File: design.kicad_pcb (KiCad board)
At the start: 2 copper layers, 28.5 x 15 mm, 15 parts, among them J1 USB_C_Receptacle, J2 Conn_01x05, Q1 2N7002K, Q2 2N7002K, Q3 2N7002K, U1 ATtiny814-SS

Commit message: update
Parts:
- moved J2 20.1 mm to (151.5, 92.5), turned to 0 degrees
- moved C1 5.79 mm to (148.2, 81.0), turned to 180 degrees
- moved C2 5.76 mm to (151.6, 81.0)
- moved U1 0.75 mm to (151.5, 86.5)
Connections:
- C1 pad 1: Net-(C1-Pad1) -> VCC
- C1 pad 2: Net-(C1-Pad2) -> GND
- C2 pad 1: Net-(C2-Pad1) -> VCC
- C2 pad 2: Net-(C2-Pad2) -> GND
- J2 pad 1: Net-(J2-Pad1) -> UDPI
- J2 pad 2: Net-(J2-Pad2) -> VCC
- J2 pad 3: Net-(J2-Pad3) -> GND
- J2 pad 4: Net-(J2-Pad4) -> TX
- J2 pad 5: Net-(J2-Pad5) -> RX
- U1 pad 1: Net-(U1-Pad1) -> VCC
- U1 pad 10: Net-(U1-Pad10) -> UDPI
- U1 pad 11: Net-(U1-Pad11) -> TX
- U1 pad 12: Net-(U1-Pad12) -> RX
- U1 pad 13: Net-(U1-Pad13) -> WS2812b
- U1 pad 14: Net-(U1-Pad14) -> GND
- U1 pad 2: Net-(U1-Pad2) -> Blue_PWM
- U1 pad 3: Net-(U1-Pad3) -> Green_PWM
- U1 pad 6: Net-(U1-Pad6) -> Red_PWM

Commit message: PCB: change usb footprint add components
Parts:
- added R4: R_Small, Resistor_SMD:R_0805_2012Metric, F.Cu at (146.9, 72.0)
- added R5: 5.1k, Resistor_SMD:R_0805_2012Metric, F.Cu at (146.9, 75.0)
- added R6: 5.1k, Resistor_SMD:R_0805_2012Metric, F.Cu at (151.3, 72.0)
- added R7: R_Small, Resistor_SMD:R_0805_2012Metric, F.Cu at (151.3, 75.0)
- added R8: R_Small, Resistor_SMD:R_0805_2012Metric, F.Cu at (155.7, 72.0)
- J1: footprint Connector_USB:USB_C_Receptacle_HRO_TYPE-C-31-M-12 -> Connector_USB:USB_C_Receptacle_HRO_TYPE-C-31-M-12_simple
- J2: footprint E32-xxxT20D:UDPI_interface -> E32-xxxT20D:UDPI_interface_small
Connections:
- J1 pad A1: Net-(J1-PadA1) -> GND
- J1 pad A12: Net-(J1-PadA1) -> GND
- J1 pad A4: Net-(J1-PadA4) -> VCC
- J1 pad A9: Net-(J1-PadA4) -> VCC
- J1 pad B1: Net-(J1-PadA1) -> GND
- J1 pad B12: Net-(J1-PadA1) -> GND
- J1 pad B4: Net-(J1-PadA4) -> VCC
- J1 pad B9: Net-(J1-PadA4) -> VCC
- J1 pad S1: Net-(J1-PadS1) -> GND
- Q1 pad 1: Red_PWM -> Net-(Q1-Pad1)
- Q2 pad 1: Green_PWM -> Net-(Q2-Pad1)
- Q3 pad 1: Blue_PWM -> Net-(Q3-Pad1)
- R1 pad 1: Red_PWM -> Net-(Q1-Pad1)
- R2 pad 1: Green_PWM -> Net-(Q2-Pad1)
- R3 pad 1: Blue_PWM -> Net-(Q3-Pad1)

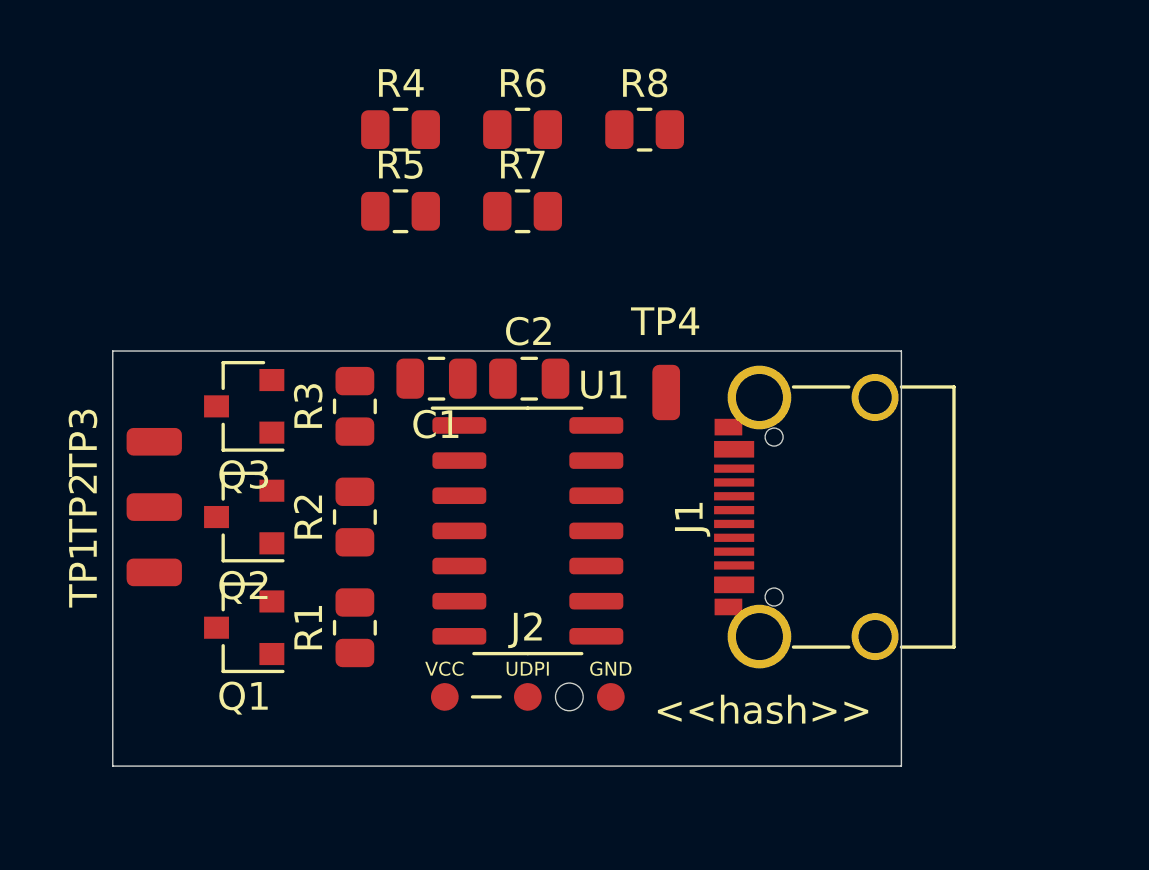
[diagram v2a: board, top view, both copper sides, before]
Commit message: PCB: move components
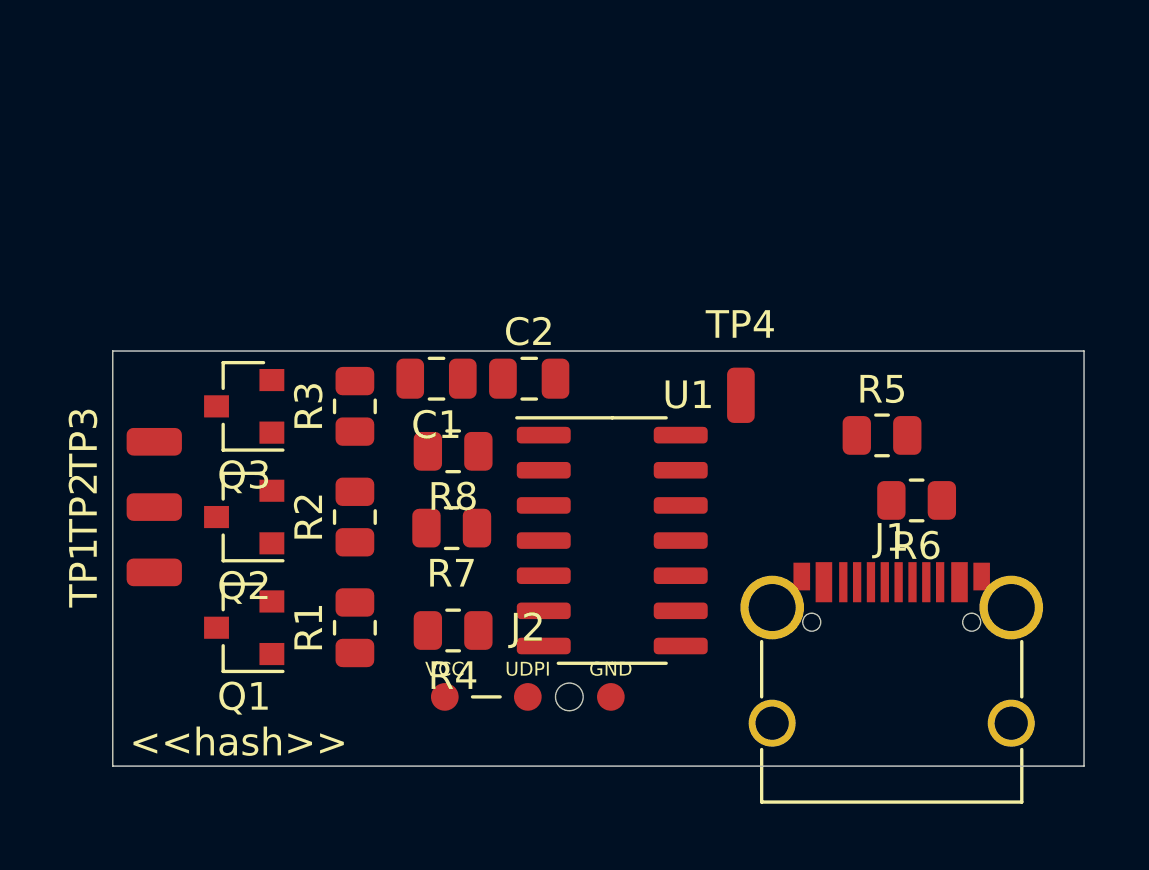
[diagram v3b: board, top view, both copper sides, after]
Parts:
- moved R6 19.6 mm to (165.6, 85.4), turned to 180 degrees
- moved R5 19.2 mm to (164.3, 83.0)
- moved R4 18.2 mm to (148.8, 90.1), turned to 180 degrees
- moved R8 13.5 mm to (148.8, 83.6), turned to 180 degrees
- moved R7 11.7 mm to (148.8, 86.4), turned to 180 degrees
- moved J1 6.61 mm to (164.7, 92.4), turned to 0 degrees
- moved U1 3.07 mm to (154.6, 86.8)
- moved TP4 2.70 mm to (159.2, 81.6)
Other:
- board size 28.5 x 15 mm -> 35.1 x 15 mm

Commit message: PCB: arrange
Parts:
- moved TP4 10.6 mm to (169.8, 81.4)
- moved C1 4.60 mm to (152.8, 81.2)
- moved C2 4.60 mm to (156.2, 81.2)
- moved J2 3.08 mm to (154.5, 93.2), turned to 180 degrees
- moved TP1 2.00 mm to (138.0, 90.0)
- moved TP3 1.28 mm to (138.0, 82.0)
- moved R5 0.50 mm to (164.3, 83.5)
- moved R6 0.50 mm to (165.6, 85.9)
- moved R8 0.43 mm to (148.8, 83.2)
- moved R4 0.42 mm to (148.7, 89.7)
- moved TP2 0.36 mm to (138.0, 86.0)
- moved R7 0.10 mm to (148.8, 86.5)
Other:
- board text added: "Blue"
- board text added: "Green"
- board text added: "Red"
- board text added: "WS2812B"
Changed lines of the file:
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@@
   (general
     (thickness 1.6)
-    (drawings 6)
+    (drawings 10)
     (tracks 0)
     (zones 0)
@@
     (47 F.CrtYd user)
     (48 B.Fab user)
-    (49 F.Fab user)
+    (49 F.Fab user hide)
   )
   (setup
@@
   )
   (module Resistor_SMD:R_0805_2012Metric (layer F.Cu)
-    (at 148.8 83.625 180)
+    (at 148.7875 83.2 180)
     (descr "Resistor SMD 0805 (2012 Metric), square (rectangular) end terminal, IPC_7351 nominal, (Body size source: IPC-SM-782 page 72, https://www.pcb-3d.com/wordpress/wp-content/uploads/ipc-sm-782a_amendment_1_and_2.pdf), generated with kicad-footprint-generator")
     (tags resistor)
@@
   )
   (module Resistor_SMD:R_0805_2012Metric (layer F.Cu)
-    (at 148.75 86.4 180)
+    (at 148.75 86.5 180)
     (descr "Resistor SMD 0805 (2012 Metric), square (rectangular) end terminal, IPC_7351 nominal, (Body size source: IPC-SM-782 page 72, https://www.pcb-3d.com/wordpress/wp-content/uploads/ipc-sm-782a_amendment_1_and_2.pdf), generated with kicad-footprint-generator")
     (tags resistor)
@@
   )
   (module Resistor_SMD:R_0805_2012Metric (layer F.Cu)
-    (at 165.55 85.4 180)
+    (at 165.55 85.9 180)
     (descr "Resistor SMD 0805 (2012 Metric), square (rectangular) end terminal, IPC_7351 nominal, (Body size source: IPC-SM-782 page 72, https://www.pcb-3d.com/wordpress/wp-content/uploads/ipc-sm-782a_amendment_1_and_2.pdf), generated with kicad-footprint-generator")
     (tags resistor)
     (attr smd)
-    (fp_text reference R6 (at 0 -1.65) (layer F.SilkS)
+    (fp_text reference R6 (at 2.65 -0.1) (layer F.SilkS)
       (effects (font (size 1 1) (thickness 0.15)))
     )
@@
   )
   (module Resistor_SMD:R_0805_2012Metric (layer F.Cu)
-    (at 164.3 83.05)
+    (at 164.3 83.55)
     (descr "Resistor SMD 0805 (2012 Metric), square (rectangular) end terminal, IPC_7351 nominal, (Body size source: IPC-SM-782 page 72, https://www.pcb-3d.com/wordpress/wp-content/uploads/ipc-sm-782a_amendment_1_and_2.pdf), generated with kicad-footprint-generator")
     (tags resistor)
     (attr smd)
-    (fp_text reference R5 (at 0 -1.65) (layer F.SilkS)
+    (fp_text reference R5 (at 2.7 -0.05) (layer F.SilkS)
       (effects (font (size 1 1) (thickness 0.15)))
     )
@@
   )
   (module Resistor_SMD:R_0805_2012Metric (layer F.Cu)
-    (at 148.8 90.1 180)
+    (at 148.6875 89.7 180)
     (descr "Resistor SMD 0805 (2012 Metric), square (rectangular) end terminal, IPC_7351 nominal, (Body size source: IPC-SM-782 page 72, https://www.pcb-3d.com/wordpress/wp-content/uploads/ipc-sm-782a_amendment_1_and_2.pdf), generated with kicad-footprint-generator")
     (tags resistor)
@@
   )
   (module E32-xxxT20D:UDPI_interface_small (layer F.Cu)
-    (at 151.5 92.5)
+    (at 154.5 93.2 180)
     (fp_text reference J2 (at 0 -2.5) (layer F.SilkS)
       (effects (font (size 1 1) (thickness 0.15)))
@@
     )
     (fp_line (start -2 0) (end -1 0) (layer F.SilkS) (width 0.12))
-    (pad "" np_thru_hole circle (at 1.5 0) (size 1 1) (drill 1) (layers *.Cu *.Mask))
-    (pad 3 smd circle (at 3 0) (size 1 1) (layers F.Cu F.Paste F.Mask)
-      (net 15 GND))
-    (pad 2 smd circle (at -3 0) (size 1 1) (layers F.Cu F.Paste F.Mask)
+    (pad "" np_thru_hole circle (at 1.5 0 180) (size 1 1) (drill 1) (layers *.Cu *.Mask))
+    (pad 3 smd circle (at 3 0 180) (size 1 1) (layers F.Cu F.Paste F.Mask)
+      (net 15 GND))
+    (pad 2 smd circle (at -3 0 180) (size 1 1) (layers F.Cu F.Paste F.Mask)
       (net 22 VCC))
-    (pad 1 smd circle (at 0 0) (size 1 1) (layers F.Cu F.Paste F.Mask)
+    (pad 1 smd circle (at 0 0 180) (size 1 1) (layers F.Cu F.Paste F.Mask)
       (net 25 UDPI))
   )
@@
     (tags "usb usb-c 2.0 pd")
     (attr smd)
-    (fp_text reference J1 (at 0 -5.645) (layer F.SilkS)
+    (fp_text reference J1 (at 6.15 -5.2) (layer F.SilkS)
       (effects (font (size 1 1) (thickness 0.15)))
     )
@@
     (tags "SOIC SO")
     (attr smd)
-    (fp_text reference U1 (at 2.75 -5.25) (layer F.SilkS)
+    (fp_text reference U1 (at 4.75 -3.85) (layer F.SilkS)
       (effects (font (size 1 1) (thickness 0.15)))
     )
@@
   )
   (module Connector_Wire:SolderWirePad_1x01_SMD_1x2mm (layer F.Cu)
-    (at 159.2 81.6)
+    (at 169.8 81.4)
     (descr "Wire Pad, Square, SMD Pad,  5mm x 10mm,")
     (tags "MesurementPoint Square SMDPad 5mmx10mm ")
     (attr virtual)
-    (fp_text reference TP4 (at 0 -2.54) (layer F.SilkS)
+    (fp_text reference TP4 (at 0 -2.54) (layer F.SilkS) hide
       (effects (font (size 1 1) (thickness 0.15)))
     )
@@
   )
   (module Connector_Wire:SolderWirePad_1x01_SMD_1x2mm (layer F.Cu)
-    (at 138 83.28 90)
+    (at 138 82 90)
     (descr "Wire Pad, Square, SMD Pad,  5mm x 10mm,")
     (tags "MesurementPoint Square SMDPad 5mmx10mm ")
@@
   )
   (module Connector_Wire:SolderWirePad_1x01_SMD_1x2mm (layer F.Cu)
-    (at 138 85.64 90)
+    (at 138 86 90)
     (descr "Wire Pad, Square, SMD Pad,  5mm x 10mm,")
     (tags "MesurementPoint Square SMDPad 5mmx10mm ")
@@
   )
   (module Connector_Wire:SolderWirePad_1x01_SMD_1x2mm (layer F.Cu)
-    (at 138 88 90)
+    (at 138 90 90)
     (descr "Wire Pad, Square, SMD Pad,  5mm x 10mm,")
     (tags "MesurementPoint Square SMDPad 5mmx10mm ")
@@
     (tags SOT-23)
     (attr smd)
-    (fp_text reference Q3 (at 0 -2.5) (layer F.SilkS)
+    (fp_text reference Q3 (at 2.75 -1.5) (layer F.SilkS)
       (effects (font (size 1 1) (thickness 0.15)))
     )
@@
     (tags SOT-23)
     (attr smd)
-    (fp_text reference Q2 (at 0 -2.5) (layer F.SilkS)
+    (fp_text reference Q2 (at 2.75 -1.5) (layer F.SilkS)
       (effects (font (size 1 1) (thickness 0.15)))
     )
@@
     (tags SOT-23)
     (attr smd)
-    (fp_text reference Q1 (at 0 -2.5) (layer F.SilkS)
+    (fp_text reference Q1 (at 2.65 -1.5) (layer F.SilkS)
       (effects (font (size 1 1) (thickness 0.15)))
     )
@@
   )
   (module Capacitor_SMD:C_0805_2012Metric (layer F.Cu)
-    (at 151.55 81)
+    (at 156.15 81.2)
     (descr "Capacitor SMD 0805 (2012 Metric), square (rectangular) end terminal, IPC_7351 nominal, (Body size source: IPC-SM-782 page 76, https://www.pcb-3d.com/wordpress/wp-content/uploads/ipc-sm-782a_amendment_1_and_2.pdf, https://docs.google.com/spreadsheets/d/1BsfQQcO9C6DZCsRaXUlFlo91Tg2WpOkGARC1WS5S8t0/edit?usp=sharing), generated with kicad-footprint-generator")
     (tags capacitor)
@@
   )
   (module Capacitor_SMD:C_0805_2012Metric (layer F.Cu)
-    (at 148.2 81 180)
+    (at 152.8 81.2 180)
     (descr "Capacitor SMD 0805 (2012 Metric), square (rectangular) end terminal, IPC_7351 nominal, (Body size source: IPC-SM-782 page 76, https://www.pcb-3d.com/wordpress/wp-content/uploads/ipc-sm-782a_amendment_1_and_2.pdf, https://docs.google.com/spreadsheets/d/1BsfQQcO9C6DZCsRaXUlFlo91Tg2WpOkGARC1WS5S8t0/edit?usp=sharing), generated with kicad-footprint-generator")
     (tags capacitor)
@@
     )
   )
+  (gr_text WS2812B (at 167.2 80.6) (layer F.SilkS)
+    (effects (font (size 0.5 0.5) (thickness 0.1)))
+  )
+  (gr_text Red (at 138 88.9) (layer F.SilkS)
+    (effects (font (size 0.5 0.5) (thickness 0.1)))
+  )
+  (gr_text Green (at 138 84.9) (layer F.SilkS)
+    (effects (font (size 0.5 0.5) (thickness 0.1)))
+  )
+  (gr_text Blue (at 138 80.9) (layer F.SilkS)
+    (effects (font (size 0.5 0.5) (thickness 0.1)))
+  )
   (dimension 15 (width 0.15) (layer Dwgs.User)
     (gr_text "15.000 mm" (at 131.45 87.5 270) (layer Dwgs.User)
@@
     (arrow2b (pts (xy 132.75 80) (xy 133.336421 81.126504)))
   )
-  (gr_text <<hash>> (at 141.05 94.15) (layer F.SilkS)
+  (gr_text <<hash>> (at 143.2 94) (layer F.SilkS)
     (effects (font (size 1 1) (thickness 0.15)))
   )
